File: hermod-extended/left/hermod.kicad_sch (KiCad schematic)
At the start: 39 parts, among them J1 USB_C_Receptacle_USB2.0, J2 Conn_01x05, J3 USB_C_Receptacle_USB2.0, Q1 AO3401A, Q2 MMUN2233LT1G, U1 STM32F072CBT6, U2 PRTR5V0U2X, U3 XC6206PxxxMR-Regulator_Linear, U4 CR2013-MI2120, U5 TXB0101

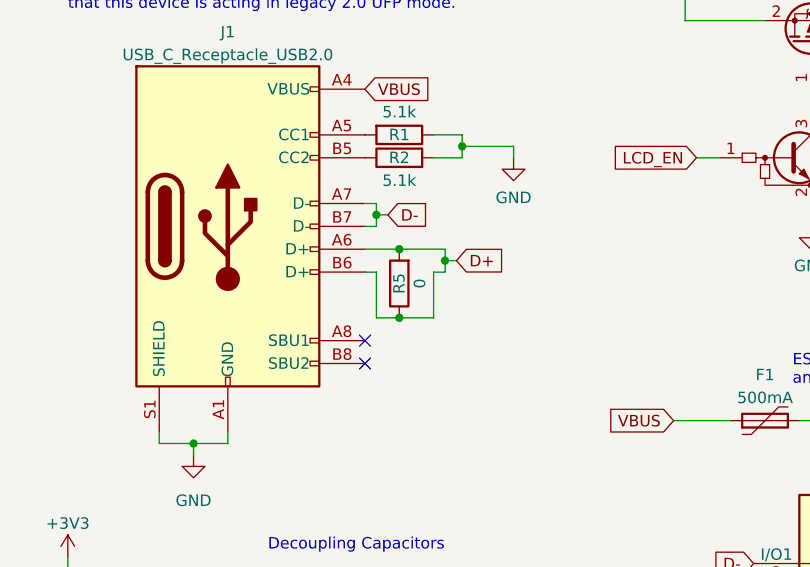
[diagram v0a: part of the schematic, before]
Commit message: Finished routing the left side 100%
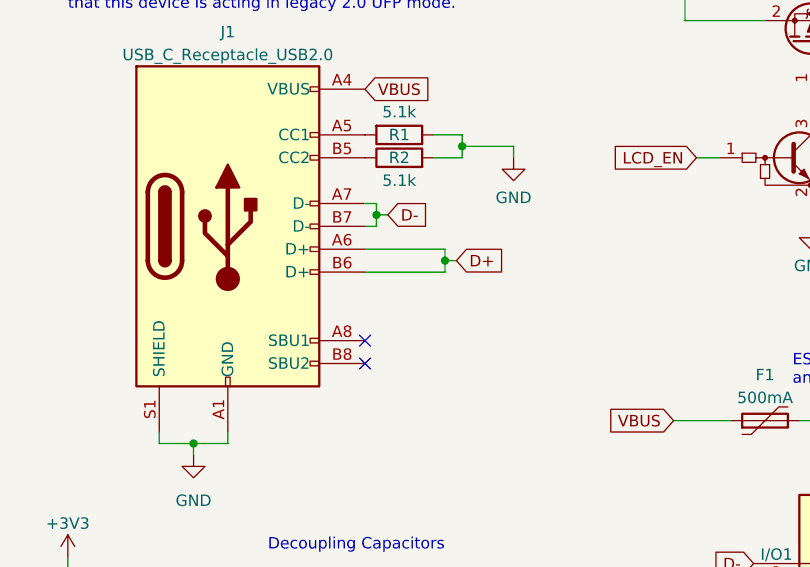
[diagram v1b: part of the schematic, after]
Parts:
- removed R5: 0, Resistor_SMD:R_0402_1005Metric, symbol Device:R
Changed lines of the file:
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@@
 	)
 	(junction
-		(at 54.61 143.51)
-		(diameter 0)
-		(color 0 0 0 0)
-	)
-	(junction
 		(at 231.14 144.145)
 		(diameter 0)
@@
 	)
 	(junction
-		(at 54.61 151.13)
-		(diameter 0)
-		(color 0 0 0 0)
-	)
-	(junction
 		(at 158.75 46.99)
 		(diameter 0)
@@
 	(wire
 		(pts
-			(xy 50.8 143.51) (xy 54.61 143.51)
+			(xy 50.8 143.51) (xy 59.69 143.51)
 		)
 		(stroke
@@
 	(wire
 		(pts
-			(xy 54.61 151.13) (xy 58.42 151.13)
-		)
-		(stroke
-			(width 0)
-			(type default)
-		)
-	)
-	(wire
-		(pts
 			(xy 194.31 146.05) (xy 193.04 146.05)
 		)
@@
 	(wire
 		(pts
-			(xy 50.8 146.05) (xy 52.07 146.05)
+			(xy 50.8 146.05) (xy 59.69 146.05)
 		)
 		(stroke
@@
 	(wire
 		(pts
-			(xy 52.07 146.05) (xy 52.07 151.13)
-		)
-		(stroke
-			(width 0)
-			(type default)
-		)
-	)
-	(wire
-		(pts
 			(xy 52.07 139.7) (xy 52.07 140.97)
 		)
@@
 	(wire
 		(pts
-			(xy 52.07 151.13) (xy 54.61 151.13)
-		)
-		(stroke
-			(width 0)
-			(type default)
-		)
-	)
-	(wire
-		(pts
 			(xy 257.81 107.95) (xy 266.7 107.95)
 		)
@@
 	(wire
 		(pts
-			(xy 54.61 143.51) (xy 59.69 143.51)
-		)
-		(stroke
-			(width 0)
-			(type default)
-		)
-	)
-	(wire
-		(pts
 			(xy 231.14 144.145) (xy 232.41 144.145)
 		)
@@
 	(wire
 		(pts
-			(xy 58.42 151.13) (xy 58.42 146.05)
-		)
-		(stroke
-			(width 0)
-			(type default)
-		)
-	)
-	(wire
-		(pts
 			(xy 26.67 59.69) (xy 36.83 59.69)
 		)
@@
 	(wire
 		(pts
-			(xy 58.42 146.05) (xy 59.69 146.05)
-		)
-		(stroke
-			(width 0)
-			(type default)
-		)
-	)
-	(wire
-		(pts
 			(xy 248.92 68.58) (xy 255.27 68.58)
 		)
@@
 					(unit 1)
 				)
-			)
-		)
-	)
-	(symbol
-		(lib_id "Device:R")
-		(at 54.61 147.32 180)
-		(unit 1)
-		(exclude_from_sim no)
-		(in_bom yes)
-		(on_board yes)
-		(dnp no)
-		(property "Reference" "R5"
-			(at 54.61 147.32 90)
-			(effects
-				(font
-					(size 1.27 1.27)
-				)
-			)
-		)
-		(property "Value" "0"
-			(at 56.896 147.32 90)
-			(effects
-				(font
-					(size 1.27 1.27)
-				)
-			)
-		)
-		(property "Footprint" "Resistor_SMD:R_0402_1005Metric"
-			(at 56.388 147.32 90)
-			(effects
-				(font
-					(size 1.27 1.27)
-				)
-				(hide yes)
-			)
-		)
-		(property "Datasheet" "~"
-			(at 54.61 147.32 0)
-			(effects
-				(font
-					(size 1.27 1.27)
-				)
-				(hide yes)
-			)
-		)
-		(property "Description" "Resistor"
-			(at 54.61 147.32 0)
-			(effects
-				(font
-					(size 1.27 1.27)
-				)
-				(hide yes)
-			)
-		)
-		(pin "1"
-		)
-		(pin "2"
-		)
-		(instances
-			(project ""
-				(path "/cb32b2da-a60d-4ed4-a57b-2c397f553171"
-					(reference "R5")
-					(unit 1)
-				)
